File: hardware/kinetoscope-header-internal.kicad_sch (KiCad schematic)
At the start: 3 parts

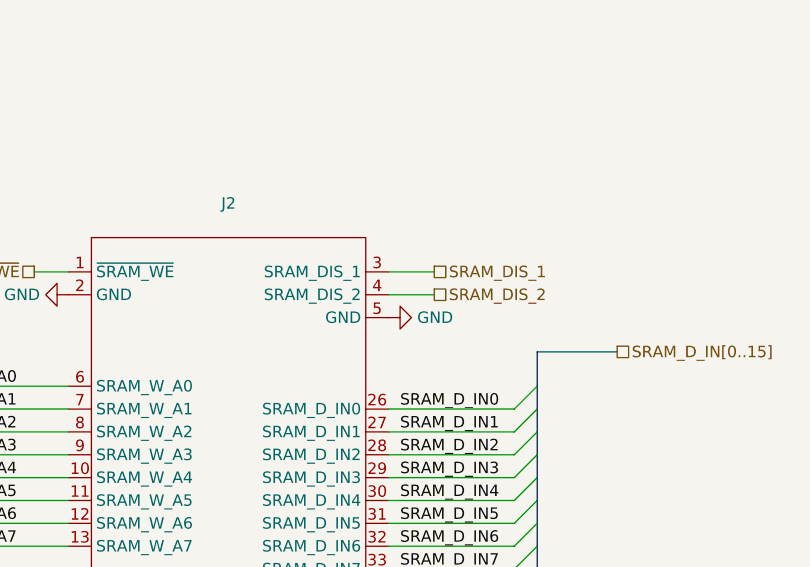
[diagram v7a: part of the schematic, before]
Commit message: Be consistent with SRAM bank numbering (0-1, not 1-2)
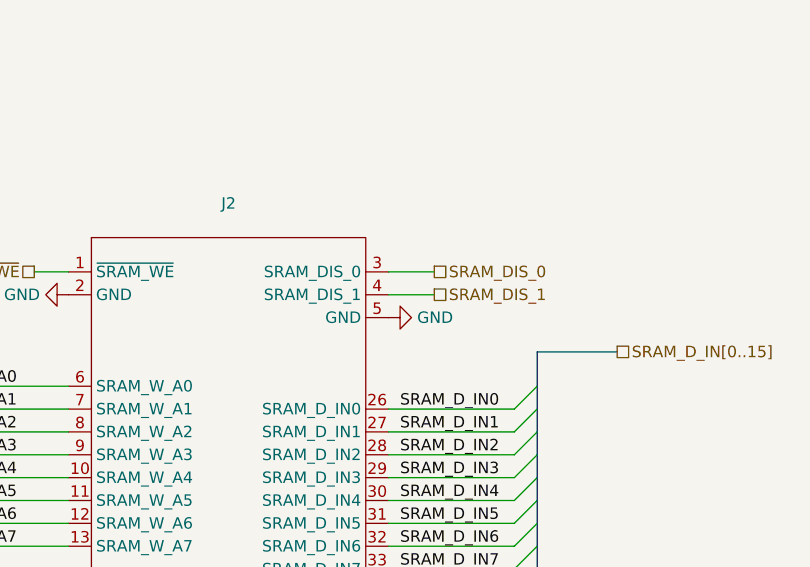
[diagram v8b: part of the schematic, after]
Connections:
- net SRAM_DIS_2 is gone; now on net SRAM_DIS_1: J2.4 (SRAM_DIS_1)
- net SRAM_DIS_1: no longer J2.3 (SRAM_DIS_1)
- new net SRAM_DIS_0: J2.3 (SRAM_DIS_0)
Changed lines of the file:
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@@
 		)
 	)
-	(hierarchical_label "SRAM_DIS_2"
+	(hierarchical_label "SRAM_DIS_1"
 		(shape passive)
 		(at 227.33 49.53 0)
@@
 		)
 	)
-	(hierarchical_label "SRAM_DIS_1"
+	(hierarchical_label "SRAM_DIS_0"
 		(shape passive)
 		(at 227.33 46.99 0)
